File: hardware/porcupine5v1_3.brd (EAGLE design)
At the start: 28.5 x 29.7 mm, 45 parts, among them X1 PROGCON

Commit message: OLED version: a) updating coil eagle package b) fixing BOM list (resistors)
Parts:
- C_OL_APP_VDD: value 10u low ESR -> 10µF/6.3V low ESR
- C_OL_VDD2: value 1u -> 1µF/16V
- C_OL_VPP: value 6.8u low ESR -> 6.8µF/16V low ESR
- L_OL: value 100uH -> 10µH
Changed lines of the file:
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@@
 <layer number="49" name="Reference" color="7" fill="1" visible="no" active="yes"/>
 <layer number="50" name="dxf" color="7" fill="1" visible="no" active="yes"/>
-<layer number="51" name="tDocu" color="7" fill="1" visible="no" active="yes"/>
-<layer number="52" name="bDocu" color="7" fill="1" visible="no" active="yes"/>
+<layer number="51" name="tDocu" color="7" fill="1" visible="yes" active="yes"/>
+<layer number="52" name="bDocu" color="7" fill="1" visible="yes" active="yes"/>
 <layer number="53" name="tGND_GNDA" color="7" fill="9" visible="no" active="no"/>
 <layer number="54" name="bGND_GNDA" color="1" fill="9" visible="no" active="no"/>
@@
 <attribute name="VALUE" x="25.9678" y="12.7872" size="0.4064" layer="27"/>
 </element>
-<element name="L_OL" library="HedgehogLib" package="1212_FOR_INDUCTANCE" value="100uH" x="23.316" y="9.0172"/>
-<element name="C_OL_APP_VDD" library="rcl" package="A/3216-18R" value="10u low ESR" x="21.0856" y="20.0098" smashed="yes">
+<element name="L_OL" library="HedgehogLib" package="1212_FOR_INDUCTANCE" value="10µH" x="23.316" y="9.0172"/>
+<element name="C_OL_APP_VDD" library="rcl" package="A/3216-18R" value="10µF/6.3V low ESR" x="21.0856" y="20.0098" smashed="yes">
 <attribute name="NAME" x="19.0848" y="20.8066" size="0.4064" layer="25"/>
 <attribute name="VALUE" x="19.0848" y="20.0978" size="0.4064" layer="27"/>
@@
 <attribute name="VALUE" x="28.0956" y="18.2622" size="0.4064" layer="27" rot="R90"/>
 </element>
-<element name="C_OL_VPP" library="rcl" package="A/3216-18R" value="6.8u low ESR" x="21.164" y="10.3462" smashed="yes">
+<element name="C_OL_VPP" library="rcl" package="A/3216-18R" value="6.8µF/16V low ESR" x="21.164" y="10.3462" smashed="yes">
 <attribute name="NAME" x="18.7822" y="11.1176" size="0.4064" layer="25"/>
 <attribute name="VALUE" x="19.722" y="9.2912" size="0.4064" layer="27"/>
@@
 <attribute name="VALUE" x="19.5768" y="23.1348" size="0.4064" layer="28" rot="MR0"/>
 </element>
-<element name="C_OL_VDD2" library="rcl" package="C0603K" value="1u" x="19.5772" y="18.2824" smashed="yes">
+<element name="C_OL_VDD2" library="rcl" package="C0603K" value="1µF/16V" x="19.5772" y="18.2824" smashed="yes">
 <attribute name="NAME" x="18.3962" y="17.383" size="0.4064" layer="25"/>
 <attribute name="VALUE" x="20.9088" y="18.1168" size="0.4064" layer="27" rot="R90"/>
@@
 </signal>
 </signals>
-<errors>
-</errors>
 </board>
 </drawing>

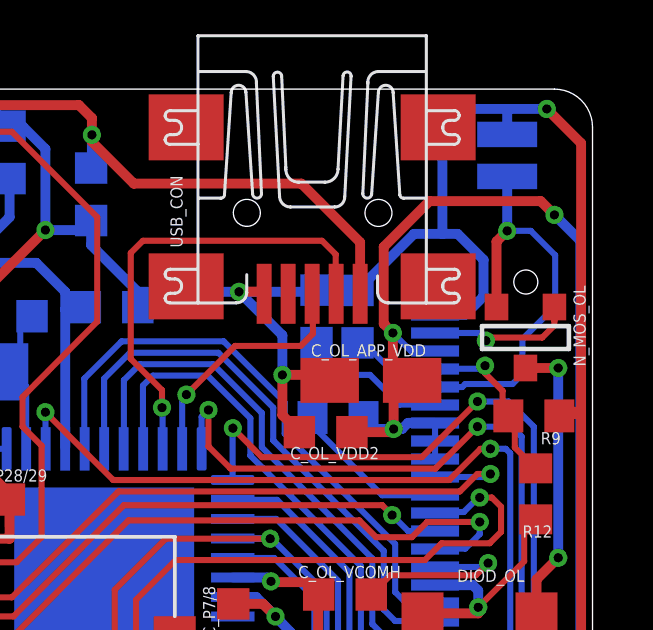
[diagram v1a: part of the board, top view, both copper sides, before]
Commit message: OLED version: improved eagle schematics
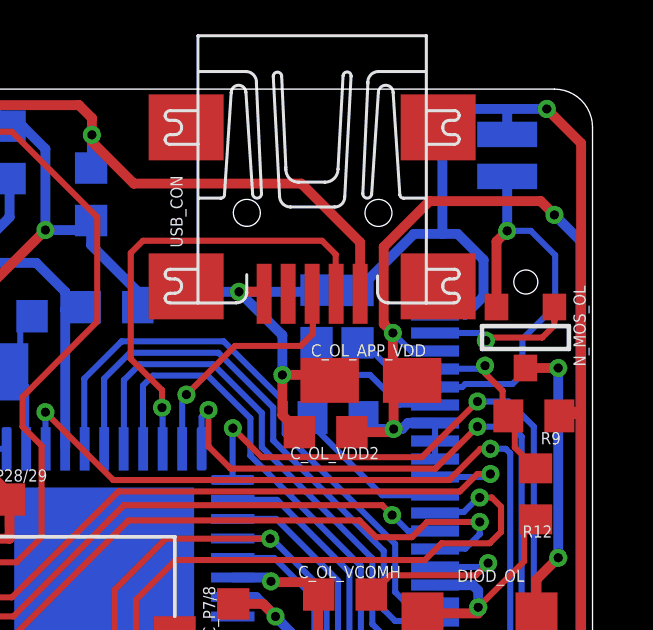
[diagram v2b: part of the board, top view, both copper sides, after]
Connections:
- net N$11 renamed OL_SW
- net N$12 renamed OL_VPP_12V
- net N$13 renamed OL_SENSE
- net N$15 renamed OL_FB
- net N$18 renamed OL_VBREF
- net N$21 renamed OL_VCOMH
- net N$30 renamed OL_IREF
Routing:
- net GND: track 194.5 -> 193.5 mm
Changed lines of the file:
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@@
 <?xml version="1.0" encoding="utf-8"?>
 <!DOCTYPE eagle SYSTEM "eagle.dtd">
-<eagle version="6.5.0">
+<eagle version="6.4">
 <drawing>
 <settings>
@@
 <contactref element="C_OL_VPP" pad="-"/>
 <contactref element="C_OL_APP_VDD" pad="-"/>
-<contactref element="CON_OLED" pad="P2"/>
 <contactref element="C_OL_VDD2" pad="1"/>
 <contactref element="C_OL_VCOMH" pad="1"/>
@@
 <wire x1="3.7338" y1="8.7376" x2="5.3982" y2="7.0732" width="0.3302" layer="1"/>
 <wire x1="5.3982" y1="7.0732" x2="5.3982" y2="5.448" width="0.3302" layer="1"/>
-<wire x1="23.2248" y1="22.1886" x2="24.2206" y2="22.1886" width="0.3302" layer="16"/>
 <wire x1="24.2206" y1="22.1886" x2="24.8412" y2="22.8092" width="0.3302" layer="16"/>
 <wire x1="24.8412" y1="22.8092" x2="24.8412" y2="24.0284" width="0.3302" layer="16"/>
 <wire x1="23.4696" y1="24.892" x2="22.5236" y2="24.892" width="0.3302" layer="16"/>
 <wire x1="23.4696" y1="29.0576" x2="23.4696" y2="24.892" width="0.3302" layer="16"/>
+<contactref element="CON_OLED" pad="P2"/>
+<wire x1="24.2206" y1="22.1886" x2="23.2248" y2="22.1886" width="0" layer="19" extent="16-16"/>
 </signal>
 <signal name="USB_D+@RC5">
@@
 <via x="27.3304" y="20.4216" extent="1-16" drill="0.3048" shape="octagon"/>
 </signal>
-<signal name="N$11">
+<signal name="OL_SW">
 <contactref element="CON_OLED" pad="P3"/>
 <contactref element="N_MOS_OL" pad="3"/>
@@
 <via x="24.9174" y="21.336" extent="1-16" drill="0.3048" shape="octagon"/>
 </signal>
-<signal name="N$12">
+<signal name="OL_VPP_12V">
 <contactref element="DIOD_OL" pad="C"/>
 <contactref element="CON_OLED" pad="P17"/>
@@
 <wire x1="26.1972" y1="15.3766" x2="26.5782" y2="15.3766" width="0.2032" layer="1"/>
 </signal>
-<signal name="N$13">
+<signal name="OL_SENSE">
 <contactref element="CON_OLED" pad="P6"/>
 <contactref element="R8" pad="P$3"/>
@@
 <via x="25.6286" y="24.9936" extent="1-16" drill="0.3048" shape="octagon"/>
 </signal>
-<signal name="N$15">
+<signal name="OL_FB">
 <contactref element="CON_OLED" pad="P5"/>
 <contactref element="R9" pad="2"/>
@@
 <via x="24.892" y="20.4978" extent="1-16" drill="0.3048" shape="octagon"/>
 </signal>
-<signal name="N$18">
+<signal name="OL_VBREF">
 <contactref element="CON_OLED" pad="P7"/>
 <contactref element="C_OL_VBREF" pad="1"/>
@@
 <wire x1="13.4948" y1="8.2984" x2="14.1478" y2="7.6454" width="0.2032" layer="16"/>
 </signal>
-<signal name="N$21">
+<signal name="OL_VCOMH">
 <contactref element="CON_OLED" pad="P16"/>
 <contactref element="C_OL_VCOMH" pad="2"/>
@@
 <wire x1="19.2024" y1="12.7508" x2="17.8638" y2="14.0894" width="0.2032" layer="16"/>
 </signal>
-<signal name="N$30">
+<signal name="OL_IREF">
 <contactref element="CON_OLED" pad="P26"/>
 <contactref element="R10" pad="2"/>
